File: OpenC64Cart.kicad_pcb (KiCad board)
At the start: 2 copper layers, 58.4 x 50.8 mm, 17 parts, among them J99 PEG_HOLE, SW1 RESET_SW, SW101 SW_Coded_SH-7010, U1 C64-Exp-Port, U101 74LS02, U102 4066, U2 27512

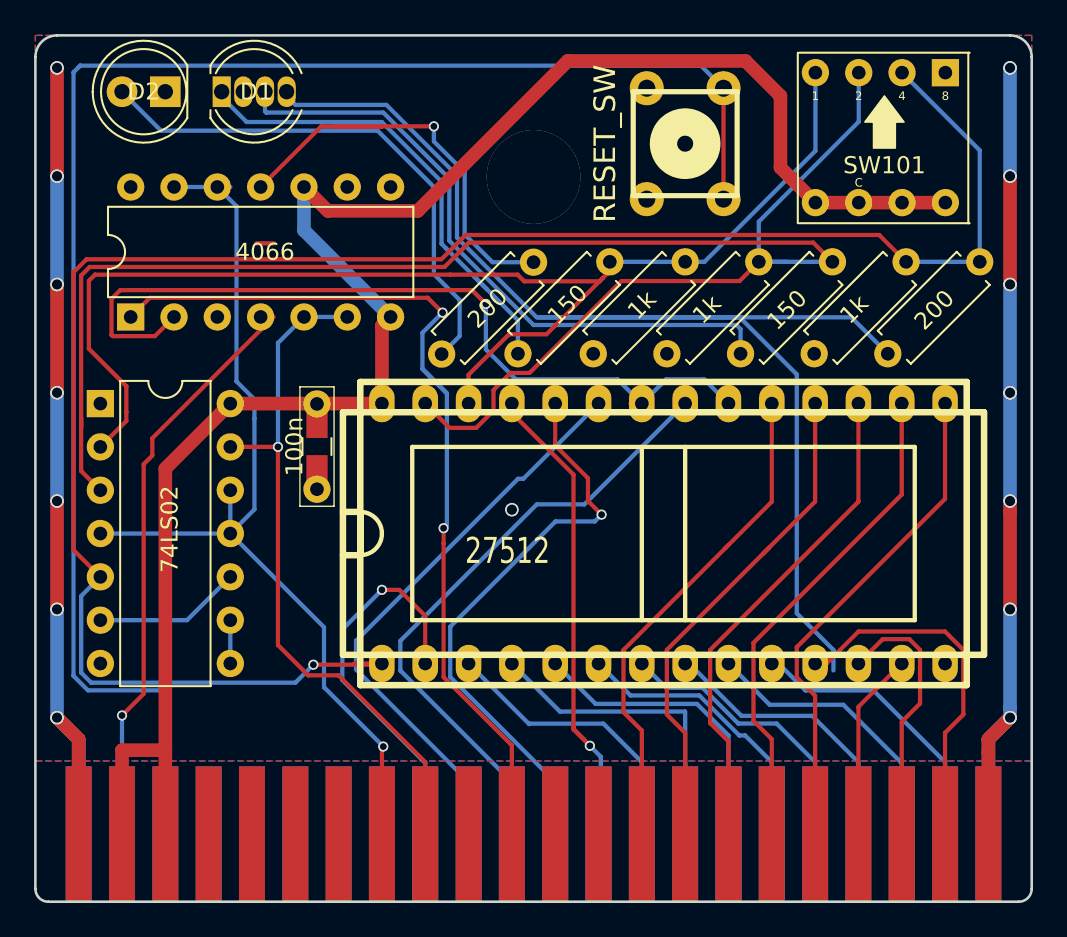
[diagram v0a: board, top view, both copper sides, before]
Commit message: Fixed Everything
This is still untested beta. I had a bunch of things wrong on my first test PCBs.
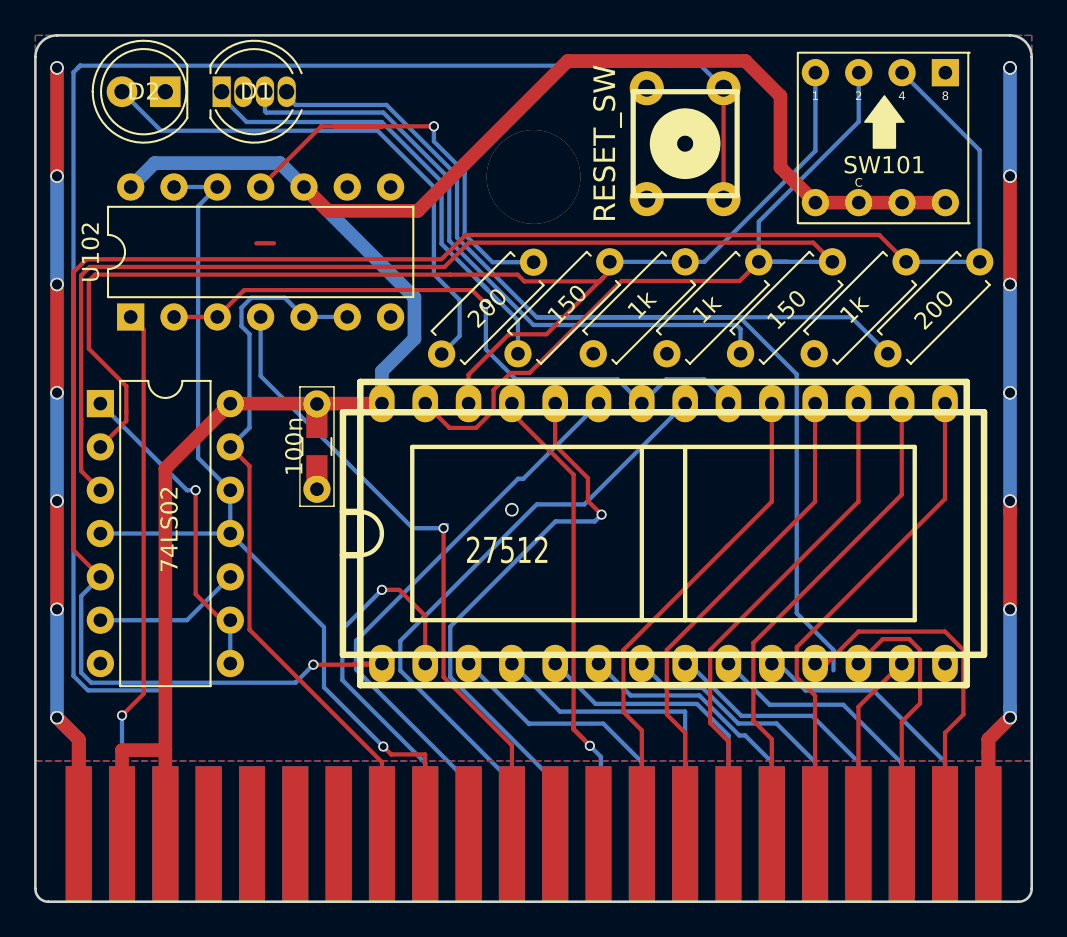
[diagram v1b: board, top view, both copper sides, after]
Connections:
- J99 pad 1: Net-(J99-Pad1) -> (no net)
- SW101 pad 8: Net-(SW101-Pad8) -> (no net)
- U1 pad 10: Net-(U1-Pad10) -> (no net)
- U1 pad 11: Net-(U1-Pad11) -> /ROML
- U1 pad 12: Net-(U1-Pad12) -> (no net)
- U1 pad 13: Net-(U1-Pad13) -> (no net)
- U1 pad 4: Net-(U1-Pad4) -> (no net)
- U1 pad 5: Net-(U1-Pad5) -> (no net)
- U1 pad 6: Net-(U1-Pad6) -> (no net)
- U1 pad 7: Net-(U1-Pad7) -> (no net)
- U1 pad 8: Net-(U1-Pad8) -> /GAME
- U1 pad 9: Net-(U1-Pad9) -> /EXROM
- U1 pad B: Net-(U1-PadB) -> /ROMH
- U1 pad D: Net-(U1-PadD) -> (no net)
- U1 pad E: Net-(U1-PadE) -> (no net)
- U1 pad F: Net-(U1-PadF) -> (no net)
- U1 pad H: Net-(U1-PadH) -> (no net)
- U1 pad J: Net-(U1-PadJ) -> (no net)
- U101 pad 11: Net-(U1-Pad8) -> /EXROM
- U101 pad 12: Net-(U1-Pad8) -> /EXROM
- U101 pad 13: Net-(U1-Pad9) -> /GAME
- U101 pad 4: Net-(U1-Pad8) -> /EXROM
- U101 pad 8: Net-(U101-Pad8) -> Net-(U101-Pad1)
- U101 pad 9: Net-(U101-Pad8) -> Net-(U101-Pad1)
- U102 pad 1: Net-(U1-Pad11) -> /ROMH
- U102 pad 12: Net-(U1-Pad8) -> /EXROM
- U102 pad 13: Net-(U1-Pad8) -> /EXROM
- U102 pad 14: GND -> +5V
- U102 pad 2: Net-(U102-Pad2) -> /CE
- U102 pad 3: Net-(U102-Pad3) -> /CE
- U102 pad 4: Net-(U1-PadB) -> /ROML
- U102 pad 5: Net-(U1-Pad9) -> /GAME
- U102 pad 6: Net-(U1-Pad9) -> /GAME
- U102 pad 7: +5V -> GND
- U102 pad 8: Net-(U102-Pad8) -> (no net)
- U102 pad 9: Net-(U102-Pad9) -> (no net)
- U2 pad 20: Net-(U102-Pad2) -> /CE
- U2 pad 22: Net-(U102-Pad2) -> /CE
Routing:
- net Net-(U1-Pad8): track 55.9 -> 0.00 mm, vias 1 -> 0
- net /EXROM: track 0.00 -> 55.4 mm, vias 0 -> 1
- net Net-(U1-Pad11): track 54.9 -> 0.00 mm, vias 2 -> 0
- net Net-(U102-Pad2): track 48.8 -> 0.00 mm, vias 1 -> 0
- net /GAME: track 0.00 -> 42.9 mm
- net Net-(U1-Pad9): track 41.6 -> 0.00 mm, vias 1 -> 0
- net /CE: track 0.00 -> 39.3 mm, vias 0 -> 1
- net /ROML: track 0.00 -> 37.8 mm, vias 0 -> 1
- net Net-(U1-PadB): track 34.0 -> 0.00 mm, vias 1 -> 0
- net /ROMH: track 0.00 -> 31.2 mm, vias 0 -> 1
- net Net-(U101-Pad1): track 0.00 -> 19.0 mm, vias 0 -> 1
- net +5V: track 107.2 -> 119.7 mm
- net Net-(U101-Pad8): track 2.54 -> 0.00 mm
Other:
- board text added: "Slot 0 Dead Test 781220 1 C64 Diag. 586220* 2 Roßmöller Doctor64 3 Trilogic 64 Doctor"
- board text added: "Slot 4 C64 Burn In 5 1541 Diagnostic 6 PSID64 Sid Player 7 586220* (SWINSID)"
- board text removed: "Slot 0 TEST1 1 TEST1 2 TEST1 3 TEST1"
- board text removed: "Slot 4 TEST1 5 TEST1 6 TEST1 7 TEST1"

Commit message: Tested
Finally received the latest revision PCB and everything is now working. I tweaked the LED resistors for the RGB LEDs I have but they may need tweaked depending on the actual specs of the LED used.
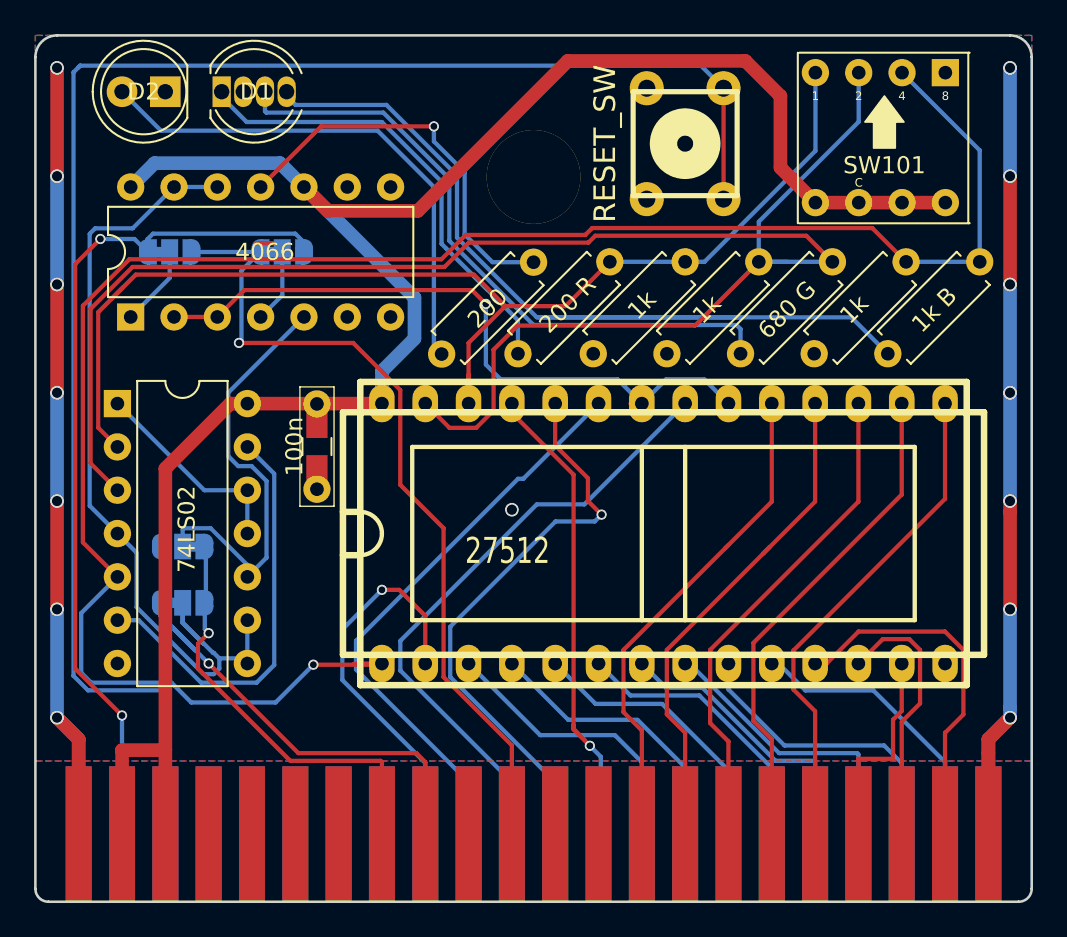
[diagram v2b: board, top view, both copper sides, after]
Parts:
- added JP1: GAME, Jumper:SolderJumper-3_P1.3mm_Bridged12_RoundedPad1.0x1.5mm_NumberLabels, B.Cu at (68.3, 108.7)
- added JP2: EXROM, Jumper:SolderJumper-3_P1.3mm_Bridged12_RoundedPad1.0x1.5mm_NumberLabels, B.Cu at (68.3, 112.0)
- added JP3: ROML, Jumper:SolderJumper-3_P1.3mm_Bridged12_RoundedPad1.0x1.5mm_NumberLabels, B.Cu at (74.2, 91.4)
- added JP4: ROMH, Jumper:SolderJumper-3_P1.3mm_Bridged12_RoundedPad1.0x1.5mm_NumberLabels, B.Cu at (67.6, 91.4)
- R1: value 150 -> 200 R
- R2: value 150 -> 680 G
- R3: value 200 -> 1k B
- moved U101 1.00 mm to (64.5, 100.3)
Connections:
- U101 pad 10: Net-(U101-Pad10) -> Net-(JP1-Pad2)
- U101 pad 11: /EXROM -> Net-(U101-Pad1)
- U101 pad 12: /EXROM -> Net-(U101-Pad1)
- U101 pad 13: /GAME -> Net-(U101-Pad13)
- U101 pad 4: /EXROM -> Net-(JP2-Pad2)
- U101 pad 6: Net-(U101-Pad10) -> Net-(U101-Pad13)
- U101 pad 8: Net-(U101-Pad1) -> Net-(JP2-Pad2)
- U101 pad 9: Net-(U101-Pad1) -> Net-(JP2-Pad2)
- U102 pad 1: /ROMH -> Net-(JP4-Pad2)
- U102 pad 12: /EXROM -> Net-(JP2-Pad2)
- U102 pad 13: /EXROM -> Net-(JP2-Pad2)
- U102 pad 4: /ROML -> Net-(JP3-Pad2)
- U102 pad 5: /GAME -> Net-(JP1-Pad2)
- U102 pad 6: /GAME -> (no net)
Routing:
- net Net-(JP2-Pad2): track 0.00 -> 50.3 mm
- net Net-(JP1-Pad2): track 0.00 -> 26.0 mm
- net Net-(U101-Pad13): track 0.00 -> 24.6 mm
- net /EXROM: track 55.4 -> 31.0 mm
- net Net-(D1-Pad4): track 78.7 -> 55.7 mm
- net /ROMH: track 31.2 -> 50.6 mm, vias 1 -> 2
- net /GAME: track 42.9 -> 25.0 mm, vias 0 -> 1
- net /ROML: track 37.8 -> 49.2 mm
- net Net-(U101-Pad10): track 8.67 -> 0.00 mm
- net Net-(U101-Pad1): track 19.0 -> 12.3 mm, vias 1 -> 0
- net Net-(U1-PadS): track 22.8 -> 16.6 mm
- net Net-(U1-PadT): track 22.0 -> 16.5 mm
- net Net-(JP4-Pad2): track 0.00 -> 4.76 mm
- net Net-(JP3-Pad2): track 0.00 -> 4.34 mm
- net /A13: track 74.2 -> 70.2 mm
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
